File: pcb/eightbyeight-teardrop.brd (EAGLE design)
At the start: 60 x 60 mm, 164 parts, among them CON1 USB_MICROSMT+THRUHULE, Q1 16MHz, SW1 SWITCH_SPDT, SW2 BRIGHTNESS, U1 MK20DN64VFM5, U10 FDG6316P, U11 FDG6316P, U12 FDG6316P, U2 ICN2026, U3 74138, U4 ICN2026, U5 MIC5219 3.3V, U6 ESP_WROOM_02, U8 MMA8653FC, U9 FDG6316P

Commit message: Rev E, as submitted
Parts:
- removed 16, 3.3V, 5, ANALOG_IN, GROUND: PTR1B2,54, testpad:B2,54
- added U$10, U$2, U$6, U$9: TEST_POINT, DevicesToMerge:IO_HOLE_3MM
- R1: value 2k 1% -> 1.6k 1%
- R12, R21, R23, R25, R26, R27, R6: value 47k -> 10k
- R13, R14, R15, R16, R2, R3, R4, R5: value 2k -> 4.7k
- moved R12 0.10 mm to (33.7, 52.5)
- moved R17 0.10 mm to (30.1, 52.5)
- moved R18 0.10 mm to (31.3, 52.5)
- moved R23 0.10 mm to (32.5, 52.5)
- moved R25 0.10 mm to (34.9, 52.5)
- moved R26 0.10 mm to (36.1, 52.5)
- renumbered BAT to J2, CON1 to J1, U$8 to U7
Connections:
- net +3V3: now also U$10.1; no longer 3.3V.TP
- net ESP_GPIO16: now also U$9.1; no longer 16.TP
- net ESP_TOUT: no longer ANALOG_IN.TP
- net EXP_GPIO5: now also U$6.1; no longer 5.TP
- net GND: now also U$2.1; no longer GROUND.TP
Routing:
- net +3V3: track 110.5 -> 98.3 mm, vias 8 -> 6
- net ESP_TOUT: track 7.15 -> 1.12 mm
- net GND: track 106.0 -> 103.2 mm, vias 103 -> 102
- net I2C_SDA: track 20.5 -> 18.1 mm
- net 1ROW7: track 122.9 -> 121.0 mm, vias 9 -> 10
- net ESP_GPIO16: track 7.84 -> 6.08 mm
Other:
- outline, holes or cut-outs redrawn
- board text added: "3.3V"
- board text added: "EightByEight RevE 2016-07"
- board text removed: "+3V"
- board text removed: "AIN"
- board text removed: "EightByEight RevD 2016-07"

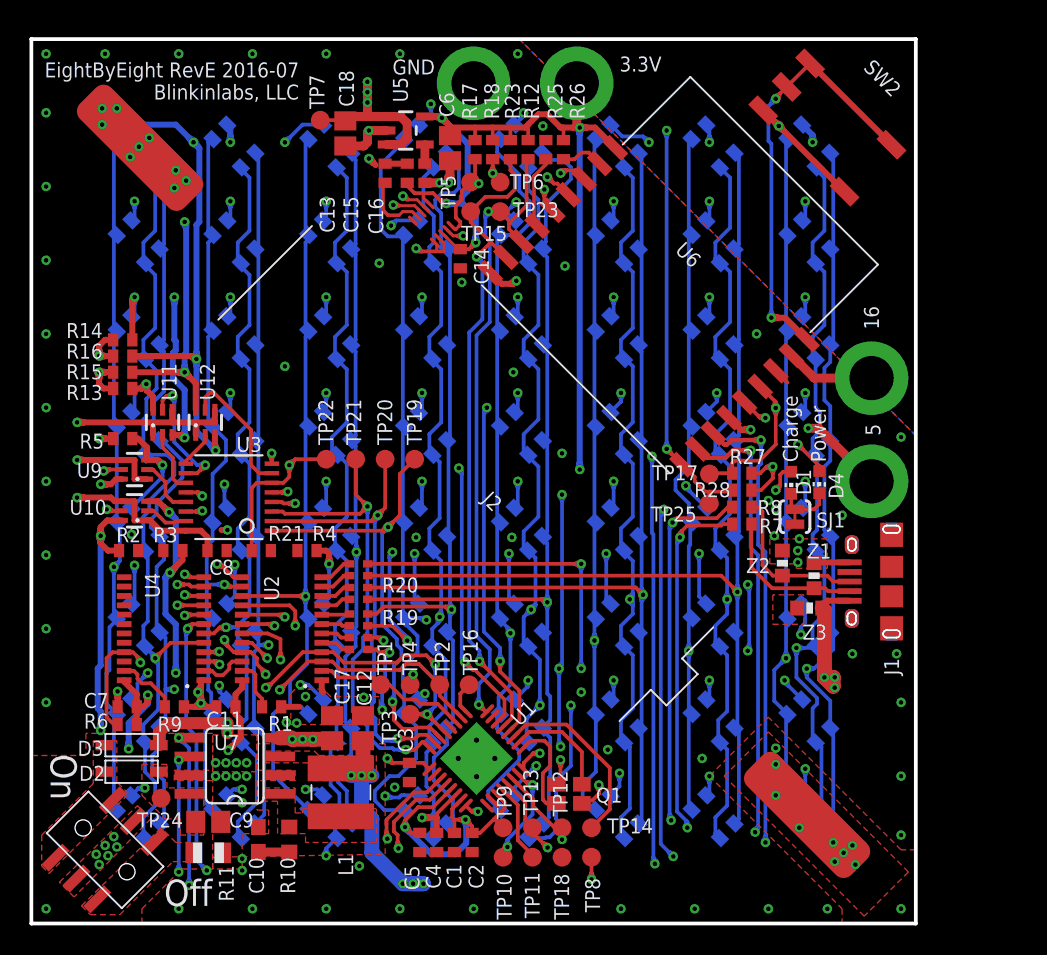
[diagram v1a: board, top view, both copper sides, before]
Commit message: Add seperate bleed resistor to 5V input
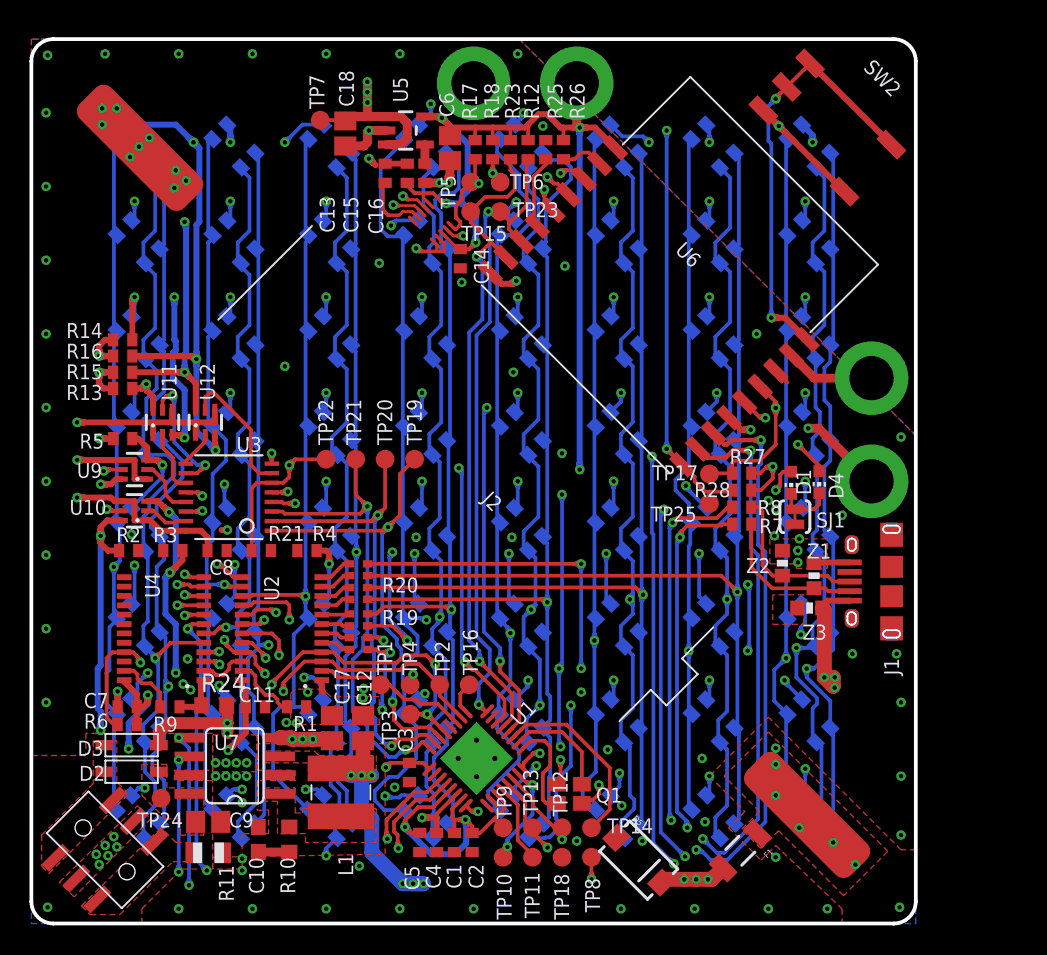
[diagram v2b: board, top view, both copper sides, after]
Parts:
- added D5: 1N5822, SparkFun-DiscreteSemi:SMA-DIODE
- added F1: PTCSMD-W, SparkFun-PowerIC:PTC-1206-WIDE
- added R24: 510, adafruit:R0603
- D2, D3: value RB161M-20 -> 1N5819
- R1: value 1.6k 1% -> 1k 1%
- R28: value DNP -> 10k
- R9: value 2k 1% -> 1k 1%
- moved C11 2.00 mm to (15.2, 14.7), turned to 0 degrees
- moved R1 1.70 mm to (18.0, 14.7)
- moved R9 0.30 mm to (9.40, 14.7)
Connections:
- new net VBAT_FUSED: C12.1, D5.C, F1.2, L1.P$1, TP8.TP, U7.3
- net GND: now also D5.A, R24.1
- net USB_5V: now also R24.2
- net VBAT: now also F1.1; no longer C12.1, L1.P$1, TP8.TP, U7.3
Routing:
- net VBAT: track 47.8 -> 0.00 mm, vias 16 -> 6
- net VBAT_FUSED: track 0.00 -> 41.7 mm, vias 0 -> 10
- net GND: track 103.2 -> 95.1 mm, vias 102 -> 109
- net DISCHARGE: track 96.1 -> 97.9 mm
- net 1ROW1: track 107.2 -> 108.5 mm
- net N$18: track 3.39 -> 4.53 mm
- net CHARGE: track 89.3 -> 90.4 mm
- net USB_5V: track 67.6 -> 68.4 mm
- net RCOL0: track 79.3 -> 80.1 mm
- net ARM_TX: track 56.6 -> 57.3 mm
- added copper zone on layer 1, net VBAT_FUSED
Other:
- outline, holes or cut-outs redrawn
- board text added: "Silk layers: 200: 2 sigma bottom (LED side) 201: 2 sigma top (component side) 203: HRC back (LED side) 204: Labels top (component side) 206: Blinkinlabs top (component side)"
- board text removed: "16"
- board text removed: "3.3V"
- board text removed: "5"
- board text removed: "Blinkinlabs, LLC"
- board text removed: "Charge"
- board text removed: "EightByEight RevE 2016-07"
- board text removed: "GND"
- board text removed: "Off"
- board text removed: "On"
- board text removed: "Power"

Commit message: Teardrop trial before release
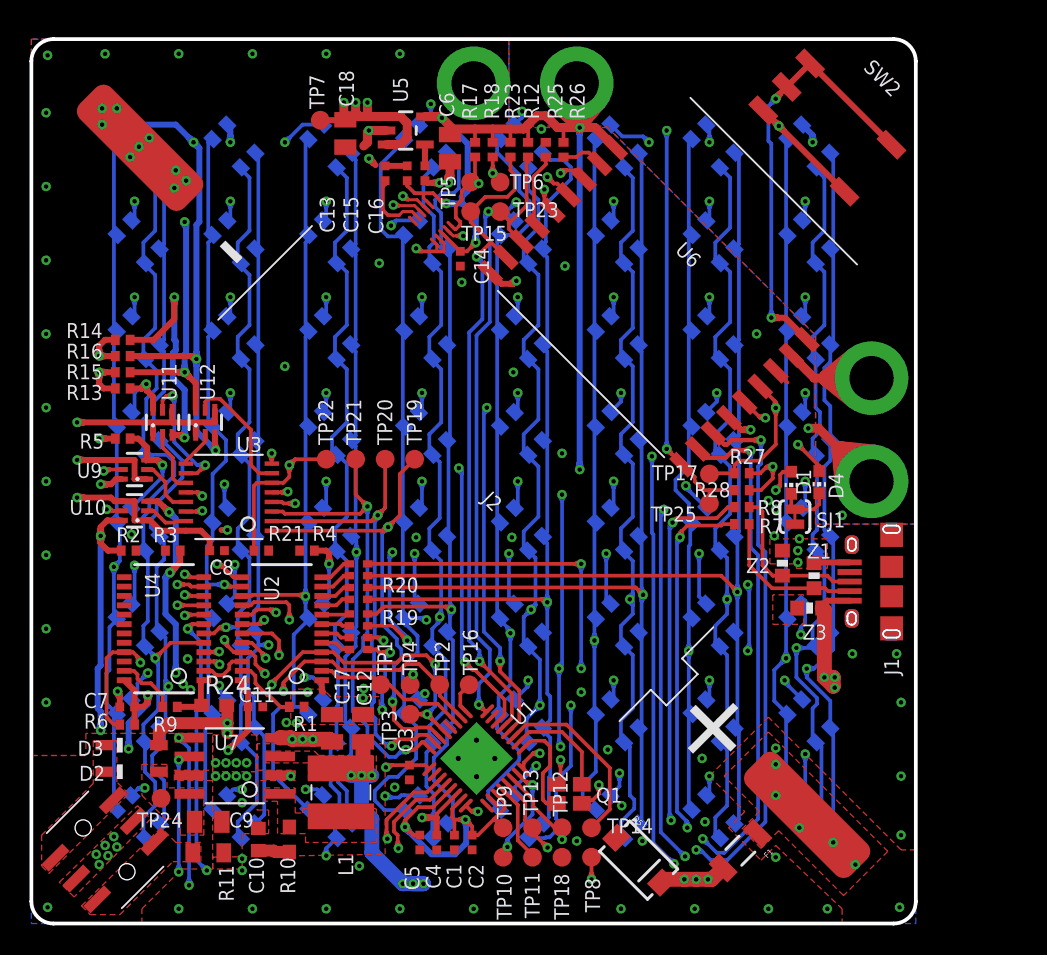
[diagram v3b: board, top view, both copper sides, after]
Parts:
- C1, C11, C13, C14, C15, C16, C2, C3, C4, C5, C7, C8: device adafruit:C0402 -> blinkinlabs:CAP_0402
- C10: device adafruit:C0603 -> blinkinlabs:CAP_0603
- C12, C17, C18, C6, C9: device adafruit:C0805 -> blinkinlabs:CAP_0805
- D2, D3: device adafruit:SOD-123 -> blinkinlabs:SOD-123
- J2: value BATTERY -> BATTERYAA_SMD
- LED_1, LED_10, LED_11, LED_12, LED_13, LED_14, LED_15, LED_16, LED_17, LED_18, LED_19, LED_2, LED_20, LED_21, LED_22, LED_23, LED_24, LED_25, LED_26, LED_27, LED_28, LED_29, LED_3, LED_30, LED_31, LED_32, LED_33, LED_34, LED_35, LED_36, LED_37, LED_38, LED_39, LED_4, LED_40, LED_41, LED_42, LED_43, LED_44, LED_45, LED_46, LED_47, LED_48, LED_49, LED_5, LED_50, LED_51, LED_52, LED_53, LED_54, LED_55, LED_56, LED_57, LED_58, LED_59, LED_6, LED_60, LED_61, LED_62, LED_63, LED_64, LED_7, LED_8, LED_9: value LED_RGB_CA -> LED_RGB_CA3528
- R1, R12, R13, R14, R15, R16, R17, R18, R2, R21, R23, R25, R26, R27, R28, R3, R4, R5, R6, R7, R8, R9: device adafruit:R0402 -> blinkinlabs:R_0402
- R10, R24: device adafruit:R0603 -> blinkinlabs:R_0603
- R11: device adafruit:R0805 -> blinkinlabs:R_0805
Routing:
- net +5V: track 144.9 -> 51.6 mm
- net USB_5V: track 68.4 -> 23.0 mm
- net VBAT_FUSED: track 41.7 -> 20.8 mm
- net EXP_GPIO5: track 14.5 -> 22.9 mm
- net ESP_GPIO16: track 6.08 -> 14.5 mm
- net +3V3: track 98.3 -> 103.3 mm
- net 1ROW5: track 102.4 -> 104.6 mm
- net 1ROW0: track 116.6 -> 118.0 mm
- net ARM_3V3: track 83.4 -> 83.9 mm
- net LED_S7: track 9.16 -> 8.65 mm
- net GND: track 95.1 -> 95.5 mm, vias 109 -> 108
- added copper zone on layer 15, net USB_5V
- added copper zone on layer 15, net VBAT_FUSED
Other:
- board text added: "+"
- board text added: "-"
- board text added: "EightByEight Blinky 2017-02-12 RevH"

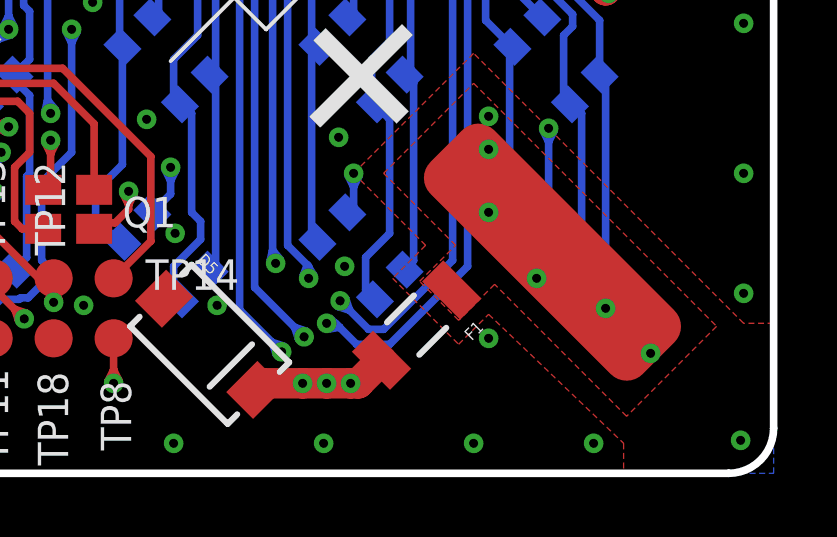
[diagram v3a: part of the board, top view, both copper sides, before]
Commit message: Switch to larger PTC, release RevH
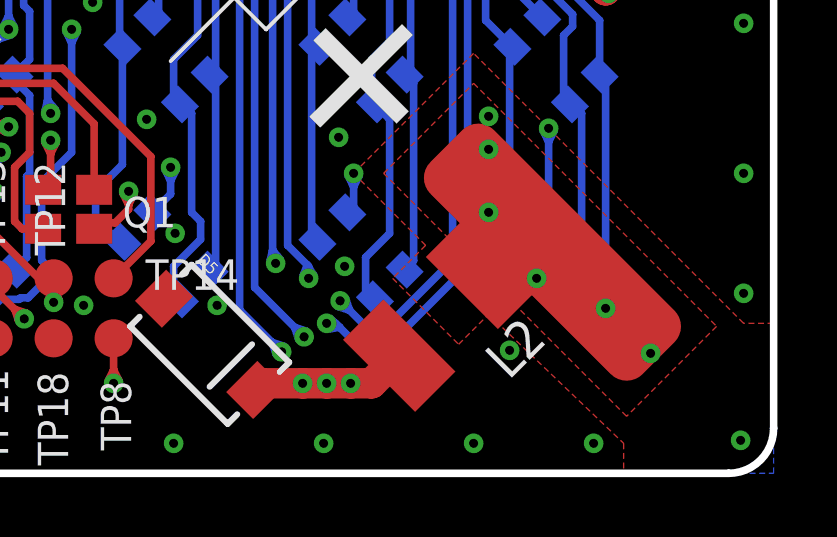
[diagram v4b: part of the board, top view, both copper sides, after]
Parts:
- removed F1: PTCSMD-W, SparkFun-PowerIC:PTC-1206-WIDE
- added L2: 1812L260THDR, rcl:L1812
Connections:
- net VBAT: now also L2.1; no longer F1.1
- net VBAT_FUSED: now also L2.2; no longer F1.2
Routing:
- net VBAT_FUSED: track 20.8 -> 21.5 mm
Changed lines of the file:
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@@
 <layer number="49" name="Reference" color="7" fill="1" visible="no" active="yes"/>
 <layer number="50" name="dxf" color="7" fill="1" visible="no" active="no"/>
-<layer number="51" name="tDocu" color="7" fill="1" visible="no" active="yes"/>
+<layer number="51" name="tDocu" color="7" fill="1" visible="yes" active="yes"/>
 <layer number="52" name="bDocu" color="7" fill="1" visible="no" active="yes"/>
 <layer number="53" name="tGND_GNDA" color="7" fill="9" visible="no" active="no"/>
@@
 <rectangle x1="2.44301875" y1="42.80666875" x2="2.54715625" y2="42.82775" layer="206"/>
 <polygon width="0.3048" layer="41">
-<vertex x="47.8" y="6.1"/>
-<vertex x="49.3" y="4.6"/>
-<vertex x="48.3" y="3.6"/>
-<vertex x="46.8" y="5.1"/>
+<vertex x="48.2" y="7"/>
+<vertex x="50.6" y="4.6"/>
+<vertex x="49.6" y="3.6"/>
+<vertex x="47.2" y="6"/>
 </polygon>
 <text x="32" y="32" size="1.4224" layer="204" font="vector" rot="R315" align="center">EightByEight Blinky
@@
 <element name="U$10" library="DevicesToMerge" package="IO_HOLE_3MM" value="TEST_POINT" x="37" y="57"/>
 <element name="D5" library="SparkFun-DiscreteSemi" package="SMA-DIODE" value="1N5822" x="41.2" y="4.3" rot="R315"/>
-<element name="F1" library="SparkFun-PowerIC" package="PTC-1206-WIDE" value="PTCSMD-W" x="48.1" y="4.94" rot="R225"/>
 <element name="R24" library="blinkinlabs" package="R_0603" value="510" x="12.4" y="14.8"/>
+<element name="L2" library="rcl" package="L1812" value="1812L260THDR" x="48.9" y="5.3" rot="R225"/>
 </elements>
 <signals>
@@
 <via x="41.45" y="5.6" extent="1-16" drill="0.3"/>
 <via x="45.7" y="6.9" extent="1-16" drill="0.3"/>
-<via x="50.5" y="4.5" extent="1-16" drill="0.3"/>
+<via x="51.2" y="4.1" extent="1-16" drill="0.3"/>
 <contactref element="R24" pad="1"/>
 <via x="18.75" y="15.7" extent="1-16" drill="0.3"/>
@@
 <via x="38" y="3" extent="1-16" drill="0.3"/>
 <contactref element="D5" pad="C"/>
-<contactref element="F1" pad="2"/>
 <wire x1="38" y1="3.450003125" x2="38" y2="3" width="0.254" layer="1"/>
 <wire x1="44.3" y1="3" x2="45.1" y2="3" width="1.016" layer="1"/>
 <wire x1="45.1" y1="3" x2="45.9" y2="3" width="1.016" layer="1"/>
-<wire x1="45.9" y1="3" x2="46.16" y2="3" width="1.016" layer="1"/>
-<wire x1="46.16" y1="3" x2="46.93044375" y2="3.77044375" width="1.016" layer="1"/>
 <wire x1="44.3" y1="3" x2="42.940559375" y2="3" width="1.016" layer="1"/>
 <wire x1="42.940559375" y1="3" x2="42.720278125" y2="2.77971875" width="1.016" layer="1"/>
@@
 <vertex x="47" y="1.5"/>
 </polygon>
+<contactref element="L2" pad="2"/>
+<wire x1="45.9" y1="3" x2="46.6" y2="3" width="1.016" layer="1"/>
+<wire x1="46.6" y1="3" x2="47.521140625" y2="3.921140625" width="1.016" layer="1"/>
 <wire x1="38" y1="3.450003125" x2="37.820296875" y2="3.089603125" width="0.254" layer="1"/>
 <wire x1="38" y1="3" x2="37.820296875" y2="3.089603125" width="0.254" layer="1"/>
@@
 <vertex x="55.1" y="1.9"/>
 <vertex x="50.7" y="6.3"/>
-<vertex x="49.5" y="5.1"/>
-<vertex x="48.2" y="6.4"/>
 <vertex x="49.4" y="7.6"/>
 <vertex x="47" y="10"/>
 </polygon>
 <contactref element="J2" pad="+"/>
-<contactref element="F1" pad="1"/>
 <via x="50.5" y="11.9" extent="1-16" drill="0.3"/>
 <via x="50.5" y="10.8" extent="1-16" drill="0.3"/>
@@
 <via x="54.4" y="5.5" extent="1-16" drill="0.3"/>
 <via x="55.9" y="4" extent="1-16" drill="0.3"/>
+<contactref element="L2" pad="1"/>
 </signal>
 </signals>
